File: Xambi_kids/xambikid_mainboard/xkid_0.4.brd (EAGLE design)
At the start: 43.8 x 29.2 mm, 18 parts

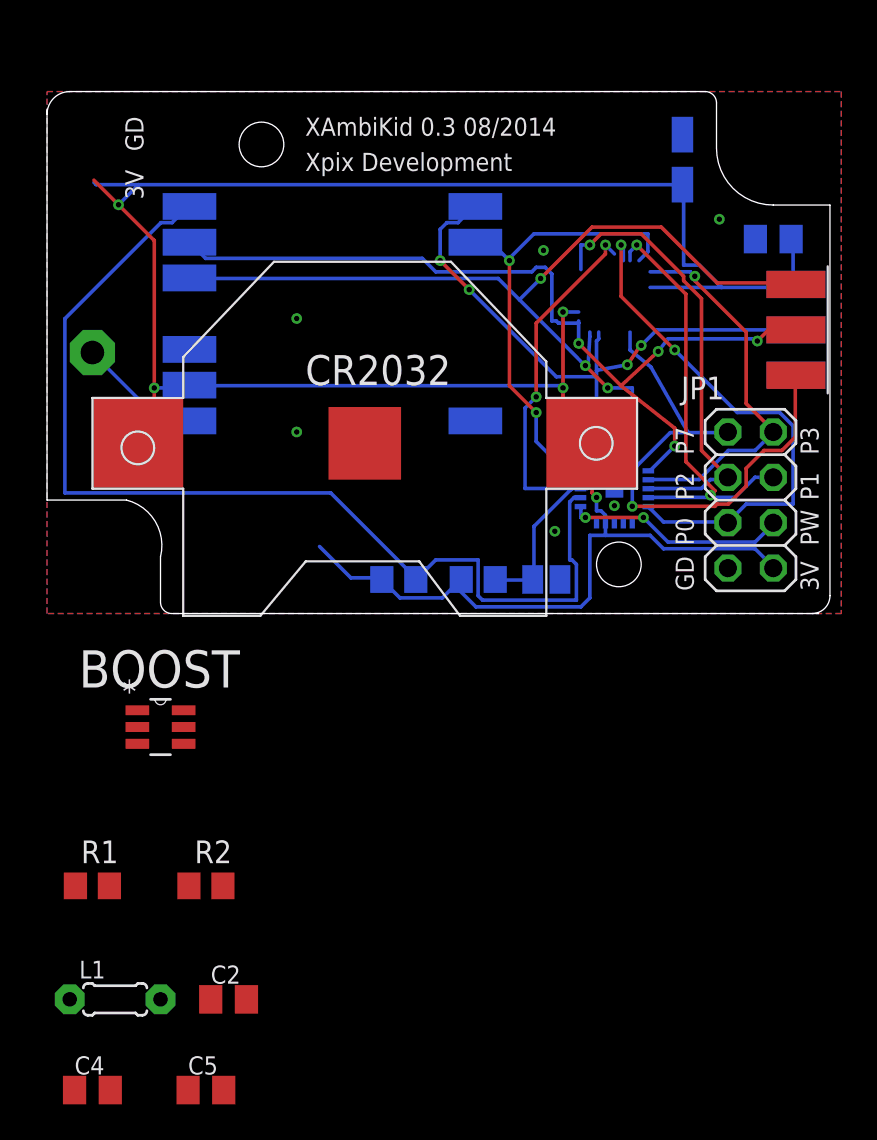
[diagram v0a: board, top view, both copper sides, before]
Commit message: - Add readme and pics to new board with booster and infrared
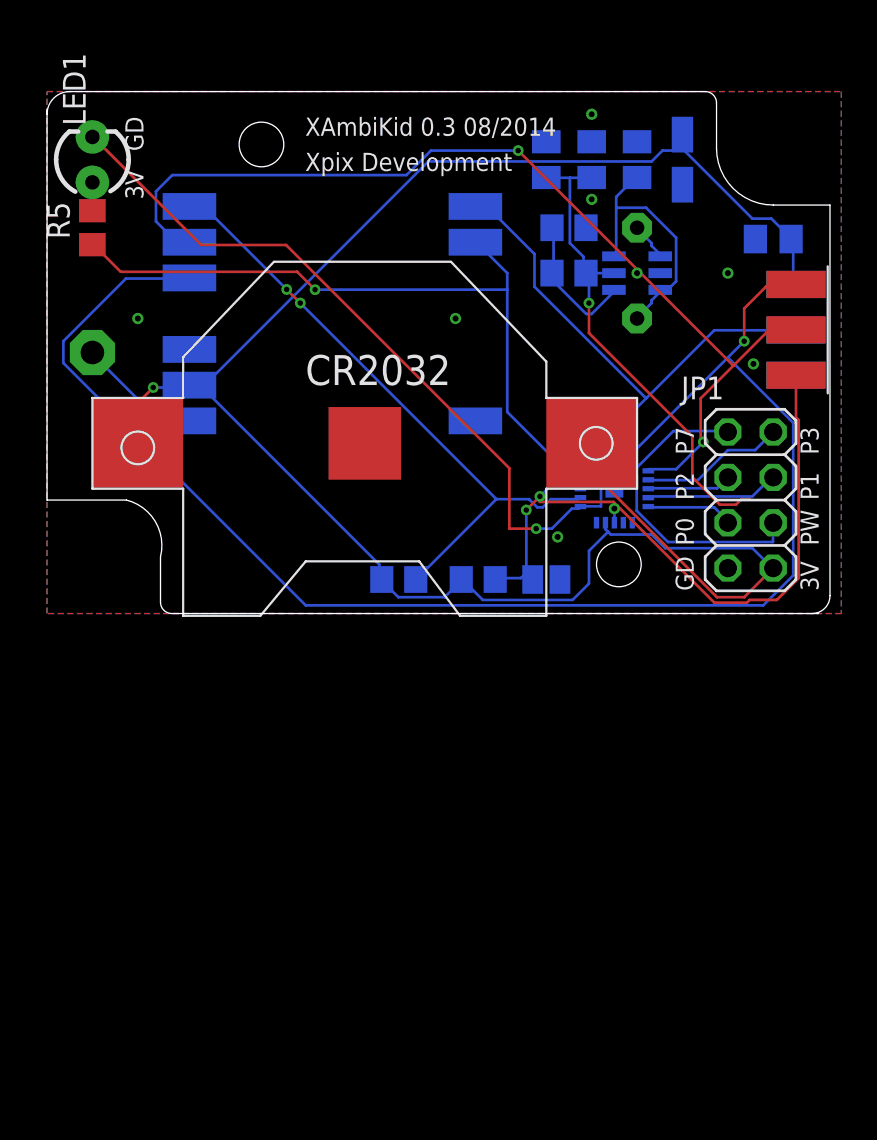
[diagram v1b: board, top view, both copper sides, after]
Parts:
- added LED1: (no value), SparkFun-LED:LED3MM
- added R5: 300R, rcl:R0805
- moved C4 59.1 mm to (30.5, 25.4), flipped to the bottom, turned to 270 degrees
- moved C5 57.4 mm to (33.0, 25.4), flipped to the bottom, turned to 270 degrees
- moved C2 50.2 mm to (27.9, 25.4), flipped to the bottom, turned to 270 degrees
- moved L1 50.0 mm to (33.0, 19.1), flipped to the bottom, turned to 270 degrees
- moved R1 45.5 mm to (29.2, 21.6), flipped to the bottom
- moved R2 39.9 mm to (29.2, 19.1), flipped to the bottom, turned to 180 degrees
- moved BOOST 36.8 mm to (33.0, 19.1), flipped to the bottom
- turned C1 to 270 degrees
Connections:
- new net ATNY_TX: JP1.6, LED1.K, TINY84.11
- new net N$1: LED1.A, R5.2
- net IRQ: now also R5.1
- net PW_RFM: no longer JP1.6, TINY84.11
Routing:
- net ATNY_TX: track 0.00 -> 55.1 mm, vias 0 -> 1
- net SDI: track 51.6 -> 84.9 mm, vias 3 -> 1
- net +3V3: track 139.5 -> 109.7 mm, vias 5 -> 1
- net PA0: track 29.8 -> 4.89 mm, vias 2 -> 0
- net SEL: track 59.0 -> 35.4 mm, vias 0 -> 2
- net PA2: track 25.4 -> 4.71 mm, vias 1 -> 0
- net PA1: track 24.5 -> 7.48 mm, vias 2 -> 0
- net PW_RFM: track 12.4 -> 27.7 mm, vias 2 -> 1
- net BAT+: track 0.00 -> 14.7 mm
- net IRQ: track 26.6 -> 40.2 mm, vias 2 -> 1
- net PA3: track 21.2 -> 8.11 mm, vias 1 -> 0
- net RST: track 47.1 -> 39.0 mm, vias 3 -> 2
- net N$4: track 0.00 -> 7.86 mm
- net SCL: track 48.1 -> 55.5 mm, vias 4 -> 2
- net PA7: track 15.9 -> 9.26 mm
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
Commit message: add booster to mainboard, add IR LED for ir communication
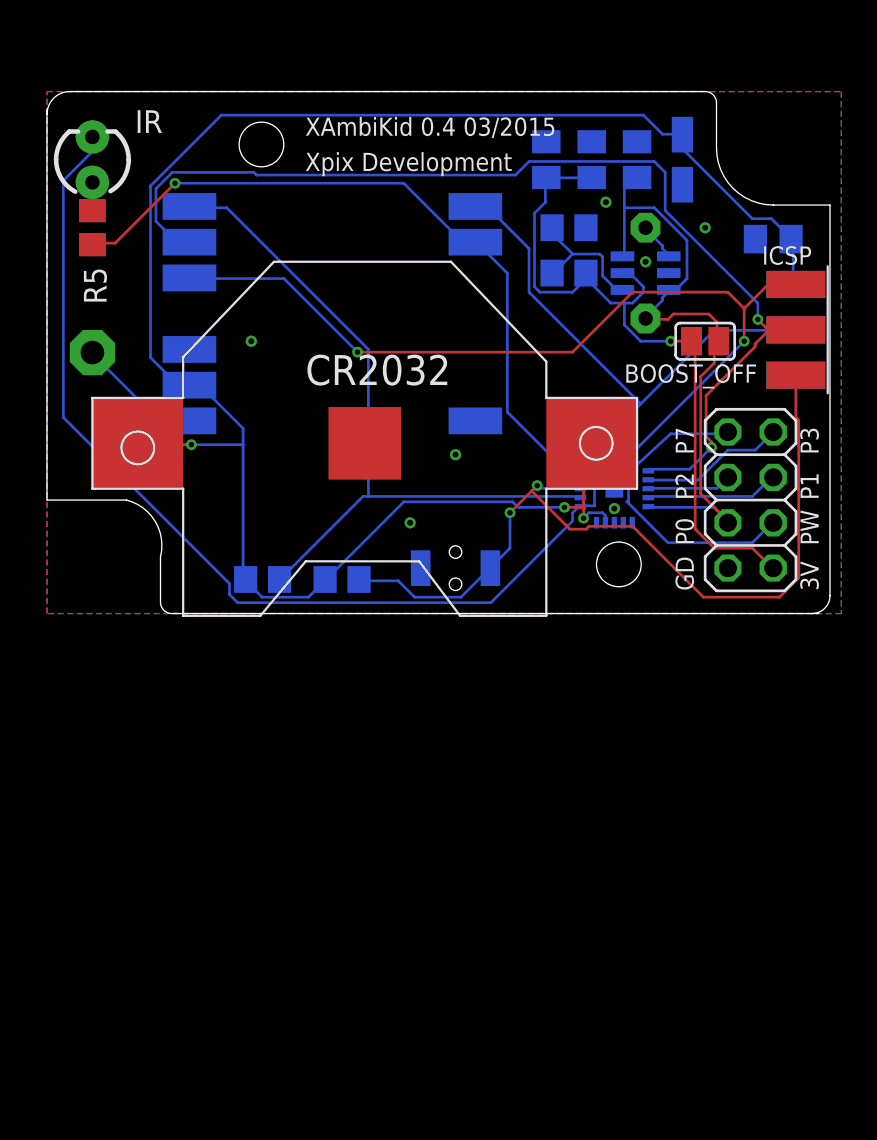
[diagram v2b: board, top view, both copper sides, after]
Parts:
- removed RESET: (no value), jumper:SJ
- added BOOST_OFF: (no value), jumper:SJ
- added S1: SWITCH-MOMENTARY-2TACTILE-SWITCH-SMD-RIGHT-ANGLE, SparkFun-Electromechanical:TACTILE_SWITCH-SMD-RIGHT-ANGLE
- IR: value (none) -> IR
- moved R3 7.62 mm to (12.1, 1.91)
- moved R4 7.62 mm to (16.5, 1.91)
- moved BOOST 0.48 mm to (33.5, 19.1)
- moved L1 0.48 mm to (33.5, 19.1)
- renumbered ANT1 to ANT, LED1 to IR
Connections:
- removed net BAT+: BOOST.3, BOOST.6, C5.2, L1.2
- removed net PW_RFM: BOOST.5, C2.2, C4.2, R2.2
- new net BOOST_POWER: BOOST.5, BOOST_OFF.2, C2.2, C4.2, JP1.8, R2.2
- net +3V3: no longer JP1.8
- net GND: now also S1.2; no longer RESET.2
- net PA0: now also BOOST.3, BOOST.6, BOOST_OFF.1, C5.2, L1.2
- net RST: now also S1.1; no longer RESET.1
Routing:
- net BOOST_POWER: track 0.00 -> 40.0 mm, vias 0 -> 1
- net SDI: track 84.9 -> 48.8 mm, vias 1 -> 2
- net PA0: track 4.89 -> 36.1 mm
- net PW_RFM: track 27.7 -> 0.00 mm, vias 1 -> 0
- net BAT+: track 14.7 -> 0.00 mm
- net ATNY_TX: track 55.1 -> 68.2 mm, vias 1 -> 0
- net +3V3: track 109.7 -> 102.3 mm, vias 1 -> 3
- net RST: track 39.0 -> 46.0 mm
- net SEL: track 35.4 -> 40.3 mm, vias 2 -> 0
- net SCL: track 55.5 -> 60.3 mm
- net GND: track 0.79 -> 0.00 mm, vias 9 -> 7
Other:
- board text added: "GND"
- board text added: "ICSP"
- board text added: "XAmbiKid 0.4 03/2015 Xpix Development"
- board text removed: "XAmbiKid 0.3 08/2014 Xpix Development"
